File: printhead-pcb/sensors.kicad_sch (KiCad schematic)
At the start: 16 parts, among them J10 T2, J11 T3, J8 T0, J9 T1, U4 ADS1015IDGS

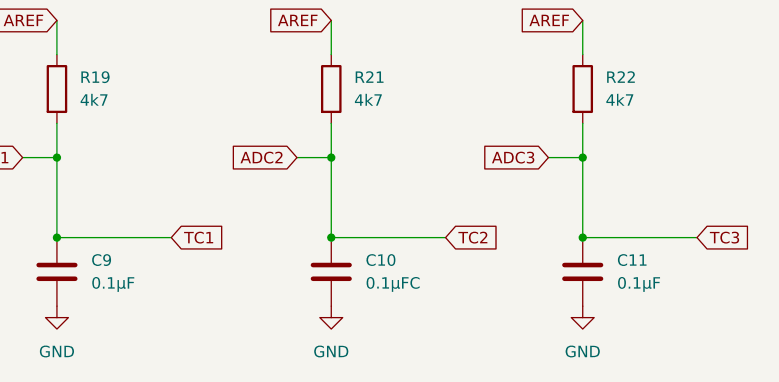
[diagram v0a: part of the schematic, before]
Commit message: implemented custom footprint
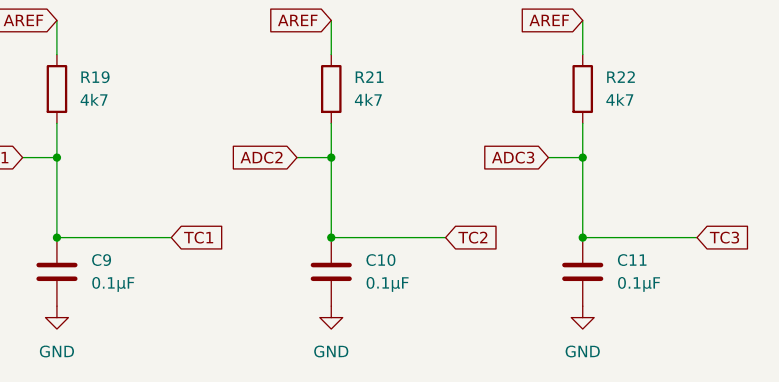
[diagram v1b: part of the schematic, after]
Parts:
- C10: value 0.1µFC -> 0.1µF
- J10, J11: footprint Connector_JST:JST_EH_B2B-EH-A_1x02_P2.50mm_Vertical -> Connector_PinHeader_2.54mm:PinHeader_1x02_P2.54mm_Horizontal
- J8, J9: footprint Connector_JST:JST_EH_S2B-EH_1x02_P2.50mm_Horizontal -> Connector_PinHeader_2.54mm:PinHeader_1x02_P2.54mm_Horizontal
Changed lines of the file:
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@@
 			)
 		)
-		(property "Footprint" "Connector_JST:JST_EH_B2B-EH-A_1x02_P2.50mm_Vertical"
+		(property "Footprint" "Connector_PinHeader_2.54mm:PinHeader_1x02_P2.54mm_Horizontal"
 			(at 151.13 69.85 0)
 			(effects
@@
 			)
 		)
-		(property "Footprint" "Connector_JST:JST_EH_S2B-EH_1x02_P2.50mm_Horizontal"
+		(property "Footprint" "Connector_PinHeader_2.54mm:PinHeader_1x02_P2.54mm_Horizontal"
 			(at 151.13 54.61 0)
 			(effects
@@
 			)
 		)
-		(property "Value" "0.1µFC"
+		(property "Value" "0.1µF"
 			(at 127 128.2699 0)
 			(effects
@@
 			)
 		)
-		(property "Footprint" "Connector_JST:JST_EH_S2B-EH_1x02_P2.50mm_Horizontal"
+		(property "Footprint" "Connector_PinHeader_2.54mm:PinHeader_1x02_P2.54mm_Horizontal"
 			(at 151.13 62.23 0)
 			(effects
@@
 			)
 		)
-		(property "Footprint" "Connector_JST:JST_EH_B2B-EH-A_1x02_P2.50mm_Vertical"
+		(property "Footprint" "Connector_PinHeader_2.54mm:PinHeader_1x02_P2.54mm_Horizontal"
 			(at 151.13 77.47 0)
 			(effects
